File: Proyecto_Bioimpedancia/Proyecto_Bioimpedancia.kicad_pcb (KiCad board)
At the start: 2 copper layers, 61 x 33.3 mm, 55 parts, among them J1 Jumper_Calibration, J2 Jumper, J3 Jumper, J4 Jumper, P1 CONN_01X03, P2 CONN_01X02, P3 CONN_01X02, P4 CONN_01X01, P5 CONN_01X01, P6 CONN_01X02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

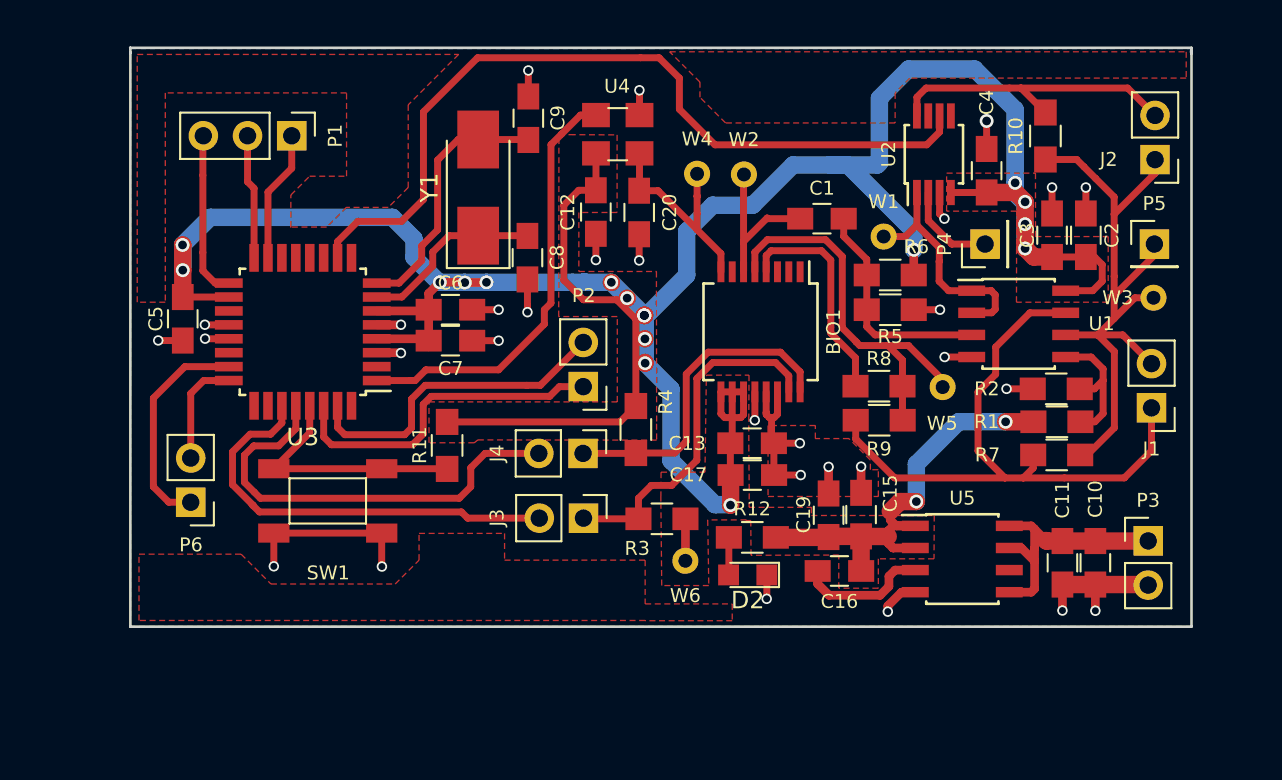
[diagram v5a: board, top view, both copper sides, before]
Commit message: Vias corregidas
Falta regulador
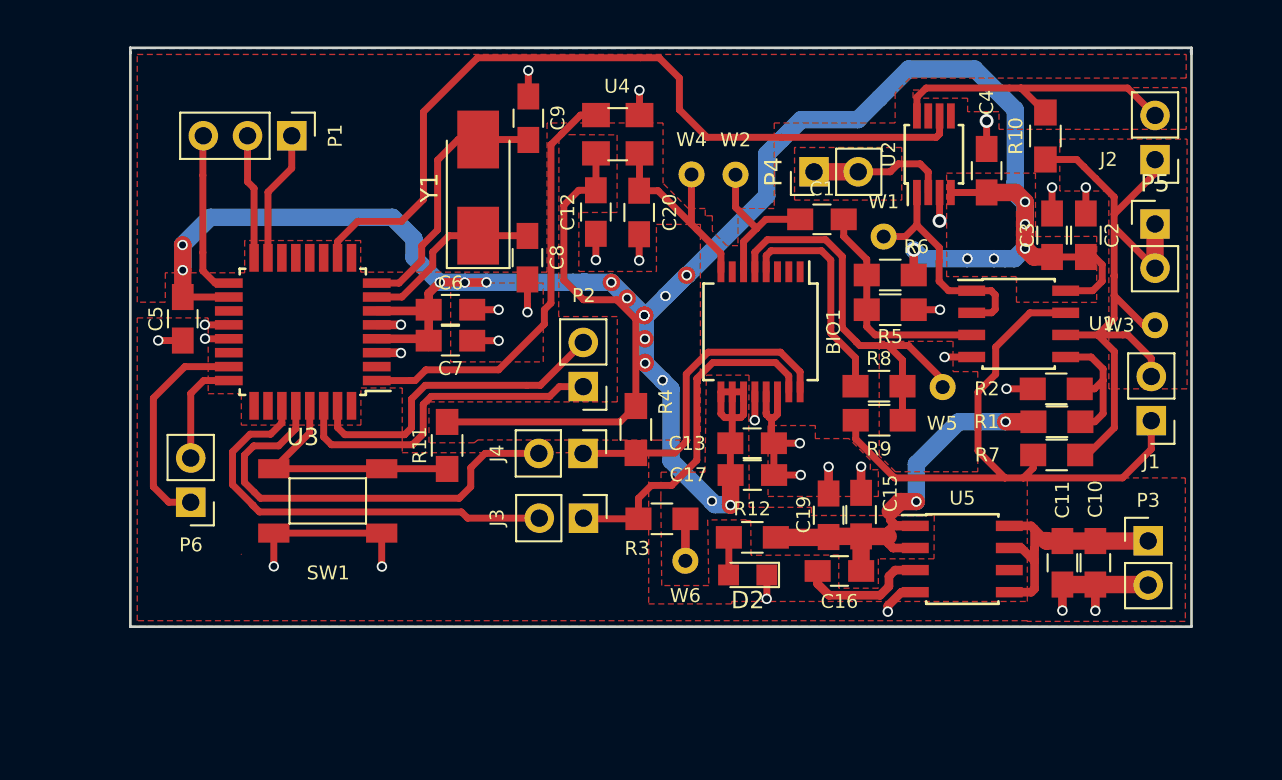
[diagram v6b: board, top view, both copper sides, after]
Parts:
- P4, P5: value CONN_01X01 -> CONN_01X02; footprint Socket_Strips:Socket_Strip_Straight_1x01_Pitch2.54mm -> Socket_Strips:Socket_Strip_Straight_1x02_Pitch2.54mm
- moved P4 10.7 mm to (215.5, 59.1)
- moved W3 1.58 mm to (235.1, 67.9)
- moved P5 1.16 mm to (235.1, 62.1)
- moved J1 0.74 mm to (234.8, 73.4)
- moved W2 0.48 mm to (211.0, 59.2)
- moved W4 0.32 mm to (208.4, 59.2)
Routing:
- net /SIGNAL_A2: track 38.3 -> 41.6 mm
- net /Z_UK: track 5.43 -> 8.13 mm
- net /3V3: track 199.0 -> 198.0 mm, vias 19 -> 24
- net /FEEDBACK_A2: track 37.1 -> 36.3 mm
- added copper zone on F.Cu, net /SIGNAL_A2
- added copper zone on F.Cu, net /VIN_AD5933
- added copper zone on F.Cu, net /Z_UK
- added copper zone on F.Cu, net Net-(J2-Pad2)

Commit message: Muescas para asegurar a la carcasa anexadas
Diseño Final Preliminar
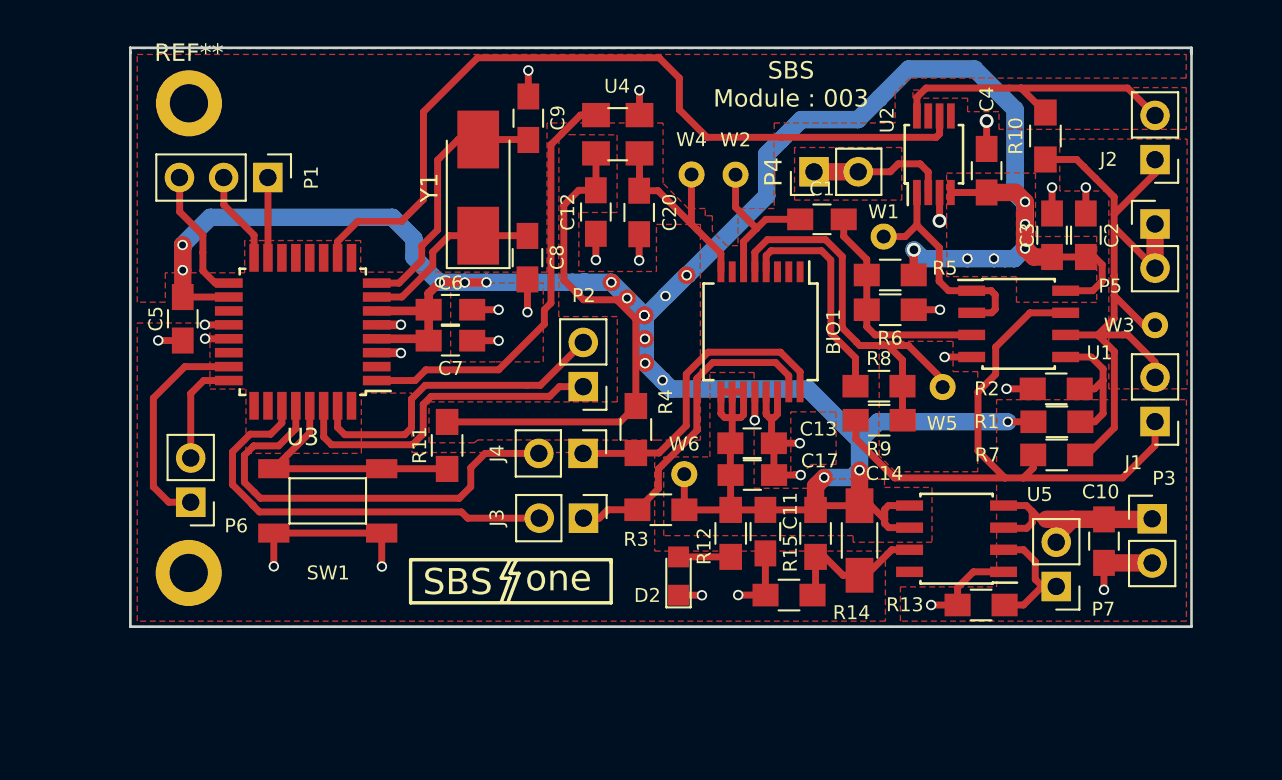
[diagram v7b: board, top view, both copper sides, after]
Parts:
- removed C15, C16: 0,1uF, Capacitors_SMD:C_0805_HandSoldering
- removed C19: 10uF, Capacitors_SMD:C_0805_HandSoldering
- added C14: 1nF, Capacitors_SMD:C_1206_HandSoldering, F.Cu at (218.1, 80.3)
- added P7: CONN_01X02, Socket_Strips:Socket_Strip_Straight_1x02_Pitch2.54mm, F.Cu at (229.4, 82.9)
- added R13: 10K, Resistors_SMD:R_0805_HandSoldering, F.Cu at (225.1, 84.0)
- added R14: 78,7K, Resistors_SMD:R_0805_HandSoldering, F.Cu at (214.0, 83.4)
- added R15: 140K, Resistors_SMD:R_0805_HandSoldering, F.Cu at (215.6, 79.9)
- added REF**: MountingHole_2.2mm_M2_DIN965_Pad, Mounting_Holes:MountingHole_2.2mm_M2_DIN965_Pad, F.Cu at (179.6, 55.1)
- added REF**: MountingHole_2.2mm_M2_DIN965_Pad, Mounting_Holes:MountingHole_2.2mm_M2_DIN965_Pad, F.Cu at (179.5, 82.1)
- C10: value 0,1uF -> 1uF
- C11: value 10uF -> 1uF
- U5: value ADP3303 -> ADP3334
- moved C11 17.2 mm to (212.7, 79.8)
- moved W6 4.98 mm to (208.0, 76.5)
- moved D2 3.98 mm to (207.7, 82.3), turned to 90 degrees
- moved P1 2.76 mm to (184.1, 59.4)
- moved C10 1.34 mm to (232.1, 80.3)
- moved P3 1.29 mm to (234.9, 79.0)
- moved R12 1.27 mm to (210.7, 79.9), turned to 270 degrees
- moved U5 1.21 mm to (223.7, 80.2), turned to 180 degrees
- moved R3 0.52 mm to (206.7, 78.5)
- moved J1 0.22 mm to (235.1, 73.4)
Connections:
- C11 pad 1: /V_FUENTE -> /3V3
- U5 pad 1: /3V3 -> /AGND
- U5 pad 2: /3V3 -> /D_REG
- U5 pad 3: Net-(C16-Pad2) -> /V_FUENTE
- U5 pad 4: /AGND -> /V_FUENTE
- U5 pad 5: /V_FUENTE -> /3V3
- U5 pad 6: Net-(U5-Pad6) -> /3V3
- U5 pad 7: /V_FUENTE -> Net-(C14-Pad1)
- U5 pad 8: /V_FUENTE -> Net-(U5-Pad8)
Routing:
- net /3V3: track 198.0 -> 209.3 mm, vias 24 -> 23
- net Net-(C14-Pad1): track 0.00 -> 8.96 mm
- net /D_REG: track 0.00 -> 7.91 mm
- net Net-(C16-Pad2): track 7.57 -> 0.00 mm
- net /MOSI: track 7.58 -> 4.62 mm
- net /V_FUENTE: track 15.1 -> 13.0 mm
- net /SCK: track 9.55 -> 7.70 mm
- net /MISO: track 7.17 -> 5.34 mm
- net /SDA: track 20.2 -> 19.2 mm
- net Net-(D2-Pad2): track 2.21 -> 3.00 mm
- net /AGND: track 64.7 -> 65.3 mm, vias 30 -> 28
- net /SCL: track 18.8 -> 18.3 mm
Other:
- board text added: "SBS"
- board text added: "SBS Module : 003"
- board text added: "one"

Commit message: Diseño Final con Planos Expandidos
Diseño 18 de Mayo
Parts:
- removed the REF** at (179.5, 82.1)
- added REF**: MountingHole_2.2mm_M2_DIN965_Pad, Mounting_Holes:MountingHole_2.7mm_M2.5_DIN965_Pad, F.Cu at (179.9, 82.6)
- REF**: footprint Mounting_Holes:MountingHole_2.2mm_M2_DIN965_Pad -> Mounting_Holes:MountingHole_2.7mm_M2.5_DIN965_Pad
- moved REF** 0.47 mm to (179.8, 54.8)
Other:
- board size 61 x 33.3 mm -> 61.1 x 34.4 mm
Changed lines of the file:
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@@
     (links 124)
     (no_connects 0)
-    (area 176.099399 51.880699 237.234801 85.292001)
+    (area 165.072814 51.359999 242.483768 88.10912)
     (thickness 1.6)
-    (drawings 23)
+    (drawings 18)
     (tracks 590)
     (zones 0)
@@
   )
   (setup
-    (last_trace_width 0.4)
+    (last_trace_width 0.1778)
     (user_trace_width 0.4)
     (user_trace_width 0.5)
@@
     (visible_elements 7FFEFFFF)
     (pcbplotparams
-      (layerselection 0x01030_80000001)
+      (layerselection 0x3ffff_80000001)
       (usegerberextensions false)
       (excludeedgelayer true)
@@
       (drillshape 0)
       (scaleselection 1)
-      (outputdirectory Gerber/))
+      (outputdirectory ../../Gerber/Andres/))
   )
   (net 0 "")
@@
     (add_net "Net-(U5-Pad8)")
   )
-  (module Mounting_Holes:MountingHole_2.2mm_M2_DIN965_Pad (layer F.Cu)
-    (at 179.5526 55.1434)
-    (descr "Mounting Hole 2.2mm, M2, DIN965")
-    (tags "mounting hole 2.2mm m2 din965")
-    (fp_text reference REF** (at 0 -2.9) (layer F.SilkS)
-      (effects (font (size 1 1) (thickness 0.15)))
-    )
-    (fp_text value MountingHole_2.2mm_M2_DIN965_Pad (at 0 2.9) (layer F.Fab)
-      (effects (font (size 1 1) (thickness 0.15)))
-    )
-    (fp_circle (center 0 0) (end 1.9 0) (layer Cmts.User) (width 0.15))
-    (fp_circle (center 0 0) (end 2.15 0) (layer F.CrtYd) (width 0.05))
-    (pad 1 thru_hole circle (at 0 0) (size 3.8 3.8) (drill 2.2) (layers *.Cu *.Mask))
+  (module Mounting_Holes:MountingHole_2.7mm_M2.5_DIN965_Pad (layer F.Cu)
+    (at 179.9336 82.5881)
+    (descr "Mounting Hole 2.7mm, M2.5, DIN965")
+    (tags "mounting hole 2.7mm m2.5 din965")
+    (fp_text reference REF** (at 5.1689 1.5494) (layer F.SilkS) hide
+      (effects (font (size 1 1) (thickness 0.15)))
+    )
+    (fp_text value MountingHole_2.2mm_M2_DIN965_Pad (at 0 3.35) (layer F.Fab)
+      (effects (font (size 1 1) (thickness 0.15)))
+    )
+    (fp_circle (center 0 0) (end 2.35 0) (layer Cmts.User) (width 0.15))
+    (fp_circle (center 0 0) (end 2.6 0) (layer F.CrtYd) (width 0.05))
+    (pad 1 thru_hole circle (at 0 0) (size 4.7 4.7) (drill 2.7) (layers *.Cu *.Mask))
   )
   (module Housings_SSOP:SSOP-16_5.3x6.2mm_Pitch0.65mm (layer F.Cu)
@@
     )
   )
-  (module Mounting_Holes:MountingHole_2.2mm_M2_DIN965_Pad (layer F.Cu)
-    (at 179.5399 82.1309)
-    (descr "Mounting Hole 2.2mm, M2, DIN965")
-    (tags "mounting hole 2.2mm m2 din965")
-    (fp_text reference REF** (at 4.953 1.651) (layer F.SilkS) hide
-      (effects (font (size 1 1) (thickness 0.15)))
-    )
-    (fp_text value MountingHole_2.2mm_M2_DIN965_Pad (at 0 2.9) (layer F.Fab)
-      (effects (font (size 1 1) (thickness 0.15)))
-    )
-    (fp_circle (center 0 0) (end 1.9 0) (layer Cmts.User) (width 0.15))
-    (fp_circle (center 0 0) (end 2.15 0) (layer F.CrtYd) (width 0.05))
-    (pad 1 thru_hole circle (at 0 0) (size 3.8 3.8) (drill 2.2) (layers *.Cu *.Mask))
-  )
+  (module Mounting_Holes:MountingHole_2.7mm_M2.5_DIN965_Pad (layer F.Cu)
+    (at 179.8193 54.7624)
+    (descr "Mounting Hole 2.7mm, M2.5, DIN965")
+    (tags "mounting hole 2.7mm m2.5 din965")
+    (fp_text reference REF** (at 5.3086 0.0254) (layer F.SilkS) hide
+      (effects (font (size 1 1) (thickness 0.15)))
+    )
+    (fp_text value MountingHole_2.2mm_M2_DIN965_Pad (at 0 3.35) (layer F.Fab)
+      (effects (font (size 1 1) (thickness 0.15)))
+    )
+    (fp_circle (center 0 0) (end 2.35 0) (layer Cmts.User) (width 0.15))
+    (fp_circle (center 0 0) (end 2.6 0) (layer F.CrtYd) (width 0.05))
+    (pad 1 thru_hole circle (at 0 0) (size 4.7 4.7) (drill 2.7) (layers *.Cu *.Mask))
+  )
+  (gr_line (start 176.1109 85.8139) (end 176.1109 51.435) (angle 90) (layer Edge.Cuts) (width 0.15))
+  (gr_line (start 176.1109 51.435) (end 237.236 51.435) (angle 90) (layer Edge.Cuts) (width 0.15))
+  (gr_line (start 237.236 85.8139) (end 176.1109 85.8139) (angle 90) (layer Edge.Cuts) (width 0.15))
+  (gr_line (start 237.236 51.435) (end 237.236 85.8139) (angle 90) (layer Edge.Cuts) (width 0.15))
   (gr_text "SBS\nModule : 003" (at 214.1474 54.0639) (layer F.SilkS)
     (effects (font (size 1 1) (thickness 0.2)))
@@
     (effects (font (size 1.5 1.5) (thickness 0.375)))
   )
-  (gr_line (start 237.1598 52.2605) (end 237.1471 52.2605) (angle 90) (layer Edge.Cuts) (width 0.15))
-  (gr_line (start 237.1598 51.9557) (end 237.1598 52.2605) (angle 90) (layer Edge.Cuts) (width 0.15))
-  (gr_line (start 176.1744 51.9557) (end 237.1598 51.9557) (angle 90) (layer Edge.Cuts) (width 0.15))
-  (gr_line (start 176.1871 51.9684) (end 176.1744 51.9557) (angle 90) (layer Edge.Cuts) (width 0.15))
-  (gr_line (start 176.1871 52.2605) (end 176.1871 51.9684) (angle 90) (layer Edge.Cuts) (width 0.15))
-  (gr_line (start 237.1344 52.2224) (end 237.1344 52.1208) (angle 90) (layer Edge.Cuts) (width 0.15))
-  (gr_line (start 176.1871 85.217) (end 176.1871 52.2224) (angle 90) (layer Edge.Cuts) (width 0.15))
-  (gr_line (start 237.1598 85.217) (end 176.1871 85.217) (angle 90) (layer Edge.Cuts) (width 0.15))
-  (gr_line (start 237.1598 52.1335) (end 237.1598 85.217) (angle 90) (layer Edge.Cuts) (width 0.15))
   (segment (start 216.4334 68.0085) (end 216.4334 68.3514) (width 0.4) (layer F.Cu) (net 1))
   (segment (start 212.7198 64.8252) (end 212.7198 63.8989) (width 0.4) (layer F.Cu) (net 1))
@@
   (segment (start 232.1306 79.0521) (end 234.8665 79.0521) (width 1) (layer F.Cu) (net 12))
   (segment (start 234.8665 79.0521) (end 234.8992 79.0194) (width 1) (layer F.Cu) (net 12))
-  (segment (start 235.0643 73.4314) (end 235.0643 74.803) (width 0.4) (layer F.Cu) (net 13) (status 400000))
+  (segment (start 235.0643 73.4314) (end 235.0643 74.803) (width 0.4) (layer F.Cu) (net 13))
   (segment (start 233.1974 76.6699) (end 234.8484 75.0189) (width 0.4) (layer F.Cu) (net 13))
   (segment (start 233.1974 76.6699) (end 227.4951 76.6699) (width 0.4) (layer F.Cu) (net 13))
@@
   (segment (start 226.441 76.6699) (end 227.4951 76.6699) (width 0.4) (layer F.Cu) (net 13))
   (segment (start 224.8916 75.1205) (end 226.441 76.6699) (width 0.4) (layer F.Cu) (net 13))
-  (segment (start 235.0643 70.8914) (end 235.0643 70.0151) (width 0.4) (layer F.Cu) (net 14) (status 400000))
+  (segment (start 235.0643 70.8914) (end 235.0643 70.0151) (width 0.4) (layer F.Cu) (net 14))
   (segment (start 233.5022 68.453) (end 234.8484 69.7992) (width 0.4) (layer F.Cu) (net 14))
   (segment (start 233.2101 68.453) (end 231.775 68.453) (width 0.4) (layer F.Cu) (net 14))
@@
     (polygon
       (pts
-        (xy 176.1998 51.9938) (xy 237.1598 51.9938) (xy 237.1598 85.1916) (xy 176.1871 85.1916) (xy 176.1871 51.9938)
+        (xy 237.1598 85.7377) (xy 176.1871 85.7377) (xy 176.1871 51.5112) (xy 237.1598 51.5112) (xy 237.1598 85.7377)
       )
     )
@@
     (polygon
       (pts
-        (xy 236.855 53.6956) (xy 220.98 53.6956) (xy 220.1291 54.5465) (xy 220.1291 56.2737) (xy 213.1822 56.2737)
+        (xy 237.1598 53.6956) (xy 220.98 53.6956) (xy 220.1291 54.5465) (xy 220.1291 56.2737) (xy 213.1822 56.2737)
         (xy 213.1822 61.1886) (xy 211.0994 61.1886) (xy 211.0994 63.3222) (xy 210.4644 63.3222) (xy 209.6262 62.484)
         (xy 209.6262 61.6077) (xy 209.2198 61.6077) (xy 209.2198 61.1886) (xy 208.2419 61.1886) (xy 206.7941 59.7408)
         (xy 206.7941 56.2737) (xy 200.1266 56.2737) (xy 200.1266 64.8462) (xy 189.4205 64.8462) (xy 189.4205 63.0301)
-        (xy 182.753 63.0301) (xy 182.753 64.8843) (xy 178.1937 64.8843) (xy 178.1937 66.5734) (xy 176.5808 66.5734)
-        (xy 176.5808 52.3367) (xy 236.855 52.3367) (xy 236.855 53.6956)
+        (xy 182.753 63.0301) (xy 182.753 64.8843) (xy 178.1937 64.8843) (xy 178.1937 66.5734) (xy 176.1871 66.5734)
+        (xy 176.1871 51.5112) (xy 237.1598 51.5112) (xy 237.1598 53.6956)
       )
     )
@@
     (polygon
       (pts
-        (xy 236.9058 71.5518) (xy 232.41 71.5518) (xy 232.41 60.1853) (xy 229.5906 60.1853) (xy 229.5906 57.2008)
-        (xy 236.9058 57.2008) (xy 236.9058 71.5518)
+        (xy 237.1598 71.5518) (xy 232.41 71.5518) (xy 232.41 60.1853) (xy 229.5906 60.1853) (xy 229.5906 57.2008)
+        (xy 237.1598 57.2008) (xy 237.1598 71.5518)
       )
     )
@@
     (polygon
       (pts
-        (xy 236.855 56.642) (xy 226.0981 56.642) (xy 226.0981 55.626) (xy 224.2947 55.626) (xy 224.2947 54.8513)
-        (xy 221.1578 54.8513) (xy 221.1578 54.3814) (xy 226.0981 54.3814) (xy 226.0981 54.2417) (xy 236.855 54.2417)
-        (xy 236.855 56.642)
+        (xy 237.1598 56.642) (xy 226.0981 56.642) (xy 226.0981 55.626) (xy 224.2947 55.626) (xy 224.2947 54.8513)
+        (xy 221.1578 54.8513) (xy 221.1578 54.3814) (xy 226.0981 54.3814) (xy 226.0981 54.2417) (xy 237.1598 54.2417)
+        (xy 237.1598 56.642)
       )
     )
@@
         (xy 180.7591 71.5645) (xy 182.8292 71.5645) (xy 182.8292 75.2602) (xy 189.4586 75.2602) (xy 189.4586 71.7931)
         (xy 192.3669 71.7931) (xy 192.3669 75.2094) (xy 206.3115 75.2094) (xy 206.3115 80.8736) (xy 219.5703 80.8736)
-        (xy 219.5703 84.8995) (xy 176.5808 84.8995) (xy 176.5808 67.7672) (xy 180.7591 67.7672) (xy 180.7591 71.5645)
+        (xy 219.5703 84.8995) (xy 220.4339 84.8995) (xy 220.4339 82.931) (xy 225.9584 82.931) (xy 225.9584 72.1741)
+        (xy 236.8677 72.1741) (xy 236.8677 85.7377) (xy 176.1871 85.7377) (xy 176.1871 67.7672) (xy 180.7591 67.7672)
+        (xy 180.7591 71.5645)
       )
     )
-  )
-  (zone (net 0) (net_name "") (layer F.Cu) (hatch edge 0.508)
-    (connect_pads yes (clearance 0.508))
-    (min_thickness 0.254)
-    (fill yes (arc_segments 16) (thermal_gap 0.508) (thermal_bridge_width 0.508))
-    (polygon
-      (pts
-        (xy 236.8677 84.8995) (xy 220.4339 84.8995) (xy 220.4339 82.931) (xy 225.9584 82.931) (xy 225.9584 72.1741)
-        (xy 236.8677 72.1741) (xy 236.8677 84.8995)
-      )
-    )
